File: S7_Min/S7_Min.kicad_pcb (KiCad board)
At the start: 4 copper layers, 124 parts, among them J1 Barrel_Jack_Switch, J2 XILINX_JTAG, Q1 DMN2020L, Q2 DMN63D8LDW, Q3 DMN63D8LDW, Q4 DMN63D8LDW, U1 TPS65581, U2 XC7S50-FTGB196, U3 REF3012, U4 QSPI_Flash_SOIC8, U5 MT47H128M16XX, X1 DSC61XX

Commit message: WIP
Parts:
- C2, C33, C45, C46, C5, R36, R37: moved to B.Cu
- moved C5 110.6 mm to (138.0, 94.2)
- moved C33 100.0 mm to (140.5, 95.5), turned to 180 degrees
- moved C2 98.6 mm to (143.0, 94.8), turned to 180 degrees
- moved C45 66.1 mm to (109.9, 93.3), turned to 270 degrees
- moved R37 65.3 mm to (109.4, 94.8), turned to 180 degrees
- moved C46 61.8 mm to (110.9, 93.3), turned to 270 degrees
- moved R36 59.6 mm to (108.9, 96.8), turned to 270 degrees
- moved C11 5.14 mm to (138.0, 96.5)
- moved C6 2.55 mm to (143.0, 97.0)
- moved C10 1.49 mm to (143.0, 93.0), turned to 270 degrees
- moved C4 1.00 mm to (143.0, 98.0)
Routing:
- net Net-(C45-Pad1): track 0.00 -> 8.08 mm, vias 0 -> 1
- net GND: track 62.3 -> 60.3 mm, vias 70 -> 71
- net +1V8: track 27.6 -> 28.7 mm
- added copper zone on B.Cu, net GND

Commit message: WIP
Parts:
- added C62: 10 uF, Capacitor_SMD:C_0805_2012Metric, F.Cu at (156.5, 35.0)
- added C63: 22 uF, Capacitor_SMD:C_0805_2012Metric, F.Cu at (156.5, 32.0)
- added C64: 0.1uF, Capacitor_SMD:C_0402_1005Metric, F.Cu at (92.0, 42.1)
- added C65: 0.1uF, Capacitor_SMD:C_0402_1005Metric, F.Cu at (88.4, 44.5)
- added C66: 0.1uF, Capacitor_SMD:C_0402_1005Metric, F.Cu at (94.9, 42.9)
- added C67: 0.1uF, Capacitor_SMD:C_0402_1005Metric, F.Cu at (91.3, 44.5)
- added D4: BAS16XV2T1G, Diode_SMD:D_SOD-523, F.Cu at (88.7, 42.3)
- added J3: HDMI_A, my_parts:hdmi_type_a_10029449-111RLF, F.Cu at (97.5, 32.0)
- added J4: Conn_02x12_Odd_Even, Connector_PinHeader_2.54mm:PinHeader_2x12_P2.54mm_Vertical, F.Cu at (82.1, 32.9)
- added R41: 47K, Resistor_SMD:R_0402_1005Metric, F.Cu at (88.4, 46.5)
- added R42: 47K, Resistor_SMD:R_0402_1005Metric, F.Cu at (88.4, 48.5)
- added R43: 47K, Resistor_SMD:R_0402_1005Metric, F.Cu at (84.1, 64.2)
- added R44: 100K, Resistor_SMD:R_0402_1005Metric, F.Cu at (91.3, 46.5)
- added R45: 10K, Resistor_SMD:R_0402_1005Metric, F.Cu at (88.4, 50.5)
- added R46: 49.9, Resistor_SMD:R_0402_1005Metric, F.Cu at (81.2, 64.2)
- added R47: 49.9, Resistor_SMD:R_0402_1005Metric, F.Cu at (97.8, 42.1)
- added R48: 49.9, Resistor_SMD:R_0402_1005Metric, F.Cu at (91.3, 48.5)
- added R49: 49.9, Resistor_SMD:R_0402_1005Metric, F.Cu at (94.2, 44.9)
- added R50: 49.9, Resistor_SMD:R_0402_1005Metric, F.Cu at (97.1, 44.9)
- added R51: 49.9, Resistor_SMD:R_0402_1005Metric, F.Cu at (100.0, 44.1)
- added R52: 49.9, Resistor_SMD:R_0402_1005Metric, F.Cu at (103.0, 42.1)
- added R53: 49.9, Resistor_SMD:R_0402_1005Metric, F.Cu at (103.0, 44.1)
- added R54: 27K, Resistor_SMD:R_0402_1005Metric, F.Cu at (100.0, 46.1)
- added R55: 2.2K, Resistor_SMD:R_0402_1005Metric, F.Cu at (94.2, 46.9)
- added R56: 2.2K, Resistor_SMD:R_0402_1005Metric, F.Cu at (97.1, 46.9)
- added R57: 10K, Resistor_SMD:R_0402_1005Metric, F.Cu at (94.2, 48.9)
- added U6: AZ1117-5.0, Package_TO_SOT_SMD:SOT-223-3_TabPin2, F.Cu at (149.4, 34.7)
- added U7: TPD12S521, Package_SO:TSSOP-38_4.4x9.7mm_P0.5mm, F.Cu at (117.0, 113.0)
- C16, C17, C18, C22, C26, C28, C29, C30, C32, RN1: moved to B.Cu
- moved J2 119.2 mm to (140.9, 115.1), turned to 90 degrees
- moved C28 103.3 mm to (140.8, 98.0), turned to 270 degrees
- moved C32 98.7 mm to (142.0, 93.0), turned to 270 degrees
- moved C29 96.2 mm to (140.0, 92.3)
- moved C30 94.5 mm to (140.8, 90.0), turned to 90 degrees
- moved RN1 93.1 mm to (139.9, 110.4), turned to 270 degrees
- moved C26 19.6 mm to (142.0, 97.0), turned to 90 degrees
- moved C16 18.8 mm to (142.0, 91.0)
- moved C22 17.2 mm to (143.0, 92.0)
- moved C18 14.9 mm to (138.0, 91.0), turned to 90 degrees
- moved C17 14.7 mm to (139.0, 91.0)
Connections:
- net Net-(U2-PadP9) renamed /Bank0_14/FPGA_DONE
- U2 pad H13: Net-(U2-PadH13) -> /Bank0_14/SYSRESET
- U2 pad H14: Net-(U2-PadH14) -> HDMI_SDA
- U2 pad K12: Net-(U2-PadK12) -> HDMI_CEC
- U2 pad M10: Net-(U2-PadM10) -> HDMI_HPD
- U2 pad M11: Net-(U2-PadM11) -> HDMI_D1+
- U2 pad M12: Net-(U2-PadM12) -> HDMI_D1-
- U2 pad M14: Net-(U2-PadM14) -> HDMI_CLK-
- U2 pad N11: Net-(U2-PadN11) -> HDMI_SCL
- U2 pad N14: Net-(U2-PadN14) -> HDMI_CLK+
- U2 pad P10: /Bank0_14/SYSRESET -> HDMI_D2+
- U2 pad P11: Net-(U2-PadP11) -> HDMI_D2-
- U2 pad P12: Net-(U2-PadP12) -> HDMI_D0+
- U2 pad P13: Net-(U2-PadP13) -> HDMI_D0-
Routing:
- net /Bank0_14/JTAG_TCK: track 0.00 -> 28.2 mm, vias 0 -> 1
- net /Bank0_14/JTAG_TMS: track 0.00 -> 16.6 mm, vias 0 -> 1
- net /Bank0_14/JTAG_TDI: track 0.00 -> 15.1 mm, vias 0 -> 1
- net GND: track 60.3 -> 74.4 mm, vias 71 -> 75
- net /Bank0_14/JTAG_TDO: track 0.00 -> 14.1 mm, vias 0 -> 1
- net +3V3: track 3.54 -> 10.8 mm, vias 5 -> 8
- net /Bank0_14/SPI_F_DQ3: track 0.00 -> 0.71 mm, vias 0 -> 1
- net /Bank0_14/SPI_F_DQ2: track 0.00 -> 0.71 mm, vias 0 -> 1
- net /Bank0_14/SPI_CS: track 0.00 -> 0.71 mm, vias 0 -> 1
- net GNDA: vias 4 -> 3
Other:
- net class Default: trace_width 0.25 -> 0.15

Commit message: WIP
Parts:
- added D5: FPGA_DONE, LED_SMD:LED_0805_2012Metric, F.Cu at (163.1, 108.5)
- added Q5: DMN2020L, Package_TO_SOT_SMD:SOT-23, F.Cu at (157.8, 105.7)
- added R58: 330, Resistor_SMD:R_0805_2012Metric_Pad1.15x1.40mm_HandSolder, F.Cu at (157.9, 108.5)
- added R59: 680, Resistor_SMD:R_0805_2012Metric_Pad1.15x1.40mm_HandSolder, F.Cu at (163.0, 104.7)
- R46, R47, R50, R51: moved to B.Cu
- moved S2 129.1 mm to (156.0, 115.2), turned to 180 degrees
- moved R16 94.5 mm to (143.5, 108.2)
- moved R17 93.0 mm to (146.0, 108.2), turned to 180 degrees
- moved J3 80.8 mm to (100.1, 112.8), turned to 270 degrees
- moved R47 77.0 mm to (118.4, 116.3)
- moved R49 75.0 mm to (120.9, 115.0), turned to 180 degrees
- moved R48 73.8 mm to (120.9, 116.1), turned to 180 degrees
- moved R52 73.3 mm to (120.9, 113.1), turned to 180 degrees
- moved R51 73.0 mm to (118.4, 114.7)
- moved R50 71.6 mm to (118.4, 113.3)
- moved R53 70.3 mm to (120.9, 112.0), turned to 180 degrees
- moved R46 65.2 mm to (118.4, 117.7)
- moved U7 2.96 mm to (114.5, 114.5), turned to 180 degrees
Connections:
- U2 pad H14: HDMI_SDA -> Net-(U2-PadH14)
- U2 pad M11: HDMI_D1+ -> HDMI_CLK+
- U2 pad M12: HDMI_D1- -> HDMI_CLK-
- U2 pad M14: HDMI_CLK- -> HDMI_SCL
- U2 pad N10: Net-(U2-PadN10) -> HDMI_D0+
- U2 pad N11: HDMI_SCL -> HDMI_D0-
- U2 pad N14: HDMI_CLK+ -> HDMI_SDA
- U2 pad P10: HDMI_D2+ -> HDMI_D1+
- U2 pad P11: HDMI_D2- -> HDMI_D1-
- U2 pad P12: HDMI_D0+ -> HDMI_D2+
- U2 pad P13: HDMI_D0- -> HDMI_D2-
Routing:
- net HDMI_D2-: track 0.00 -> 55.5 mm, vias 0 -> 2
- net HDMI_D2+: track 0.00 -> 55.4 mm, vias 0 -> 2
- net HDMI_CLK+: track 0.00 -> 54.3 mm, vias 0 -> 2
- net HDMI_CLK-: track 0.00 -> 54.3 mm, vias 0 -> 2
- net HDMI_D0-: track 0.00 -> 53.0 mm, vias 0 -> 2
- net HDMI_D0+: track 0.00 -> 53.0 mm, vias 0 -> 2
- net HDMI_D1+: track 0.00 -> 52.7 mm, vias 0 -> 2
- net HDMI_D1-: track 0.00 -> 52.5 mm, vias 0 -> 2
- net /Bank0_14/PROGRAM_B: track 0.00 -> 33.2 mm
- net /Bank0_14/FPGA_DONE: track 0.00 -> 20.7 mm
- net GND: track 74.4 -> 89.6 mm, vias 75 -> 87
- net /Bank0_14/INIT_B: track 0.00 -> 8.08 mm
- net +3V3: track 10.8 -> 15.5 mm, vias 8 -> 10
- net Net-(Q5-Pad3): track 0.00 -> 4.10 mm
- net Net-(D5-Pad2): track 0.00 -> 3.80 mm

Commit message: wip
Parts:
- added H1: MountingHole_Pad, MountingHole:MountingHole_3.2mm_M3_Pad_Via, F.Cu at (96.1, 59.8)
- added H2: MountingHole_Pad, MountingHole:MountingHole_3.2mm_M3_Pad_Via, F.Cu at (165.1, 59.8)
- added H3: MountingHole_Pad, MountingHole:MountingHole_3.2mm_M3_Pad_Via, F.Cu at (165.1, 126.8)
- added H4: MountingHole_Pad, MountingHole:MountingHole_3.2mm_M3_Pad_Via, F.Cu at (96.1, 126.8)
- C64, D4, R41, R42, R43, R44, R54, R55, R56, R57: moved to B.Cu
- moved C65 81.8 mm to (123.4, 118.5)
- moved C64 79.9 mm to (115.2, 118.5), turned to 90 degrees
- moved C67 76.9 mm to (108.4, 119.5)
- moved C66 76.8 mm to (108.4, 118.5)
- moved R45 75.3 mm to (120.8, 118.5)
- moved R41 72.7 mm to (120.9, 111.5), turned to 180 degrees
- moved C14 72.6 mm to (112.8, 61.7), turned to 180 degrees
- moved L1 70.7 mm to (112.1, 77.2), turned to 180 degrees
- moved U1 70.6 mm to (115.4, 67.5), turned to 90 degrees
- moved R42 68.8 mm to (117.1, 111.0)
- moved L2 68.6 mm to (110.2, 58.2), turned to 180 degrees
- moved R44 68.5 mm to (117.1, 110.0)
- moved D4 65.9 mm to (106.3, 105.8), turned to 90 degrees
- moved R54 62.9 mm to (106.3, 108.6), turned to 90 degrees
- moved R55 62.5 mm to (104.3, 108.6), turned to 90 degrees
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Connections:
- net Net-(C13-Pad1) renamed /Power/SW1
- net Net-(C14-Pad1) renamed /Power/SW2
- net Net-(C15-Pad1) renamed /Power/SW3
- C7 pad 1: Net-(C7-Pad1) -> +12V
- C8 pad 1: Net-(C7-Pad1) -> +12V
- C9 pad 1: Net-(C7-Pad1) -> +12V
- U1 pad 1: Net-(C7-Pad1) -> +12V
- U1 pad 2: Net-(C7-Pad1) -> +12V
- U2 pad K12: HDMI_CEC -> Net-(U2-PadK12)
- U2 pad L12: Net-(U2-PadL12) -> HDMI_CEC
- U2 pad M13: Net-(U2-PadM13) -> HDMI_SCL
- U2 pad M14: HDMI_SCL -> Net-(U2-PadM14)
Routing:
- net HDMI_CEC: track 0.00 -> 43.7 mm, vias 0 -> 3
- net HDMI_SCL: track 0.00 -> 40.9 mm, vias 0 -> 3
- net HDMI_SDA: track 0.00 -> 38.5 mm, vias 0 -> 3
- net HDMI_HPD: track 0.00 -> 33.7 mm, vias 0 -> 3
- net +3V3: track 15.5 -> 41.9 mm, vias 10 -> 15
- net GND: track 89.6 -> 108.2 mm, vias 87 -> 94
- net /Externals/HDMI_C_CEC: track 0.00 -> 13.9 mm, vias 0 -> 1
- net /Externals/HDMI_C_SCL: track 0.00 -> 13.1 mm, vias 0 -> 1
- net /Externals/HDMI_C_HPD: track 0.00 -> 12.9 mm, vias 0 -> 1
- net /Externals/HDMI_C_SDA: track 0.00 -> 12.6 mm, vias 0 -> 1
- net +1V0: track 9.19 -> 15.6 mm
- net /Externals/HDMI_C_5V: track 0.00 -> 4.62 mm, vias 0 -> 2
- net +5V: track 0.00 -> 4.02 mm, vias 0 -> 2
- net Net-(R45-Pad1): track 0.00 -> 3.02 mm
- net Net-(C66-Pad2): track 0.00 -> 2.71 mm
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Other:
- board outline added: 78 x 76 mm

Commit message: WIP
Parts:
- C37, C39, C40, C41, C42, C43, C44: moved to B.Cu
- S3: value CFG_RESET -> SYS_RESET
- moved C37 116.1 mm to (154.6, 97.6)
- moved C41 107.7 mm to (146.0, 94.0), turned to 180 degrees
- moved C42 102.0 mm to (147.0, 98.0)
- moved C39 94.8 mm to (155.7, 95.3)
- moved C40 94.3 mm to (153.1, 95.2)
- moved C44 93.4 mm to (146.0, 100.0), turned to 180 degrees
- moved R7 87.4 mm to (121.9, 56.5), turned to 270 degrees
- moved C43 85.1 mm to (147.0, 97.0)
- moved R4 74.6 mm to (122.9, 59.9)
- moved R5 69.8 mm to (117.9, 78.7), turned to 90 degrees
- moved C25 69.3 mm to (127.1, 56.3), turned to 270 degrees
- moved R2 64.9 mm to (119.0, 75.3)
- moved C19 60.2 mm to (108.7, 82.0), turned to 180 degrees
- moved C21 58.4 mm to (124.8, 56.3), turned to 270 degrees
- moved C23 56.5 mm to (108.7, 80.0), turned to 180 degrees
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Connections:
- U2 pad J12: /Bank0_14/RGB2_G -> /Bank0_14/RGB2_B
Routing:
- net Net-(R4-Pad1): track 0.00 -> 10.4 mm
- net Net-(C13-Pad2): track 0.00 -> 3.41 mm
- net /Externals/HDMI_C_CEC: track 13.9 -> 17.1 mm
- net /Externals/HDMI_C_HPD: track 12.9 -> 16.1 mm
- net /Externals/HDMI_C_SCL: track 13.1 -> 16.3 mm
- net /Externals/HDMI_C_SDA: track 12.6 -> 15.7 mm
- net Net-(C15-Pad2): track 0.00 -> 3.03 mm
- net Net-(C14-Pad2): track 0.00 -> 3.03 mm
- net Net-(R1-Pad1): track 0.00 -> 3.00 mm, vias 0 -> 2
- net GND: track 108.2 -> 105.8 mm, vias 94 -> 89
- net /Externals/HDMI_C_5V: track 4.62 -> 2.92 mm, vias 2 -> 1
- net Net-(R3-Pad1): track 0.00 -> 1.50 mm, vias 0 -> 1
- net HDMI_CEC: track 43.7 -> 44.9 mm
- net HDMI_D0-: track 53.0 -> 54.1 mm
- net HDMI_D2-: track 55.5 -> 56.6 mm
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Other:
- board size 78 x 76 mm -> 78 x 72 mm
- net class Default: via_drill 0.3 -> 0.25
- net class HDMI_DIFF added: clearance 0.1, trace_width 0.15, via_dia 0.45, via_drill 0.2
- net class Power: via_drill 0.3 -> 0.25

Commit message: WIP
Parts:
- C35, C36, RN2: moved to B.Cu
- moved U4 91.5 mm to (143.8, 78.2)
- moved C36 88.9 mm to (144.1, 77.5), turned to 180 degrees
- moved R27 88.1 mm to (150.1, 77.6)
- moved R33 86.7 mm to (141.5, 84.0)
- moved R29 85.3 mm to (137.5, 77.6), turned to 180 degrees
- moved R28 85.2 mm to (137.5, 78.9), turned to 180 degrees
- moved C35 76.8 mm to (144.1, 76.3), turned to 180 degrees
- moved C20 42.5 mm to (142.6, 62.0), turned to 0 degrees
- moved C24 40.8 mm to (142.6, 64.3), turned to 0 degrees
- moved C27 39.3 mm to (142.6, 66.7), turned to 0 degrees
- moved R6 29.3 mm to (136.1, 60.9), turned to 180 degrees
- moved R3 26.7 mm to (132.7, 59.8), turned to 90 degrees
- moved L2 25.4 mm to (135.5, 65.3), turned to 0 degrees
- moved R7 23.9 mm to (136.1, 75.7), turned to 180 degrees
- moved L3 22.9 mm to (135.5, 71.3), turned to 0 degrees
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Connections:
- RN2 pad 1: /Bank0_14/SPI_DQ0 -> /Bank0_14/SPI_DQ2
- RN2 pad 2: /Bank0_14/SPI_DQ1 -> /Bank0_14/SPI_DQ3
- RN2 pad 3: /Bank0_14/SPI_DQ2 -> /Bank0_14/SPI_DQ0
- RN2 pad 4: /Bank0_14/SPI_DQ3 -> /Bank0_14/SPI_DQ1
- RN2 pad 5: /Bank0_14/SPI_F_DQ3 -> /Bank0_14/SPI_F_DQ1
- RN2 pad 6: /Bank0_14/SPI_F_DQ2 -> /Bank0_14/SPI_F_DQ0
- RN2 pad 7: /Bank0_14/SPI_F_DQ1 -> /Bank0_14/SPI_F_DQ3
- RN2 pad 8: /Bank0_14/SPI_F_DQ0 -> /Bank0_14/SPI_F_DQ2
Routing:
- net /Bank0_14/SPI_CS: track 0.71 -> 21.5 mm, vias 1 -> 2
- net /Bank0_14/SPI_SCLK: track 0.00 -> 12.7 mm
- net /Bank0_14/SPI_DQ3: track 0.00 -> 12.4 mm, vias 0 -> 1
- net /Bank0_14/SPI_DQ1: track 0.00 -> 9.96 mm, vias 0 -> 1
- net /Bank0_14/SPI_DQ2: track 0.00 -> 9.87 mm, vias 0 -> 1
- net +3V3: track 41.9 -> 48.5 mm, vias 14 -> 16
- net /Bank0_14/SPI_DQ0: track 0.00 -> 6.50 mm, vias 0 -> 1
- net GND: track 105.8 -> 111.3 mm, vias 89 -> 91
- net /Bank0_14/SPI_F_DQ2: track 0.71 -> 5.91 mm
- net /Bank0_14/SPI_F_DQ1: track 0.00 -> 4.12 mm, vias 0 -> 1
- net /Bank0_14/SPI_F_SCLK: track 0.00 -> 4.01 mm
- net /Bank0_14/SPI_F_DQ3: track 0.71 -> 4.71 mm
- net /Bank0_14/SPI_F_DQ0: track 0.00 -> 3.91 mm, vias 0 -> 1

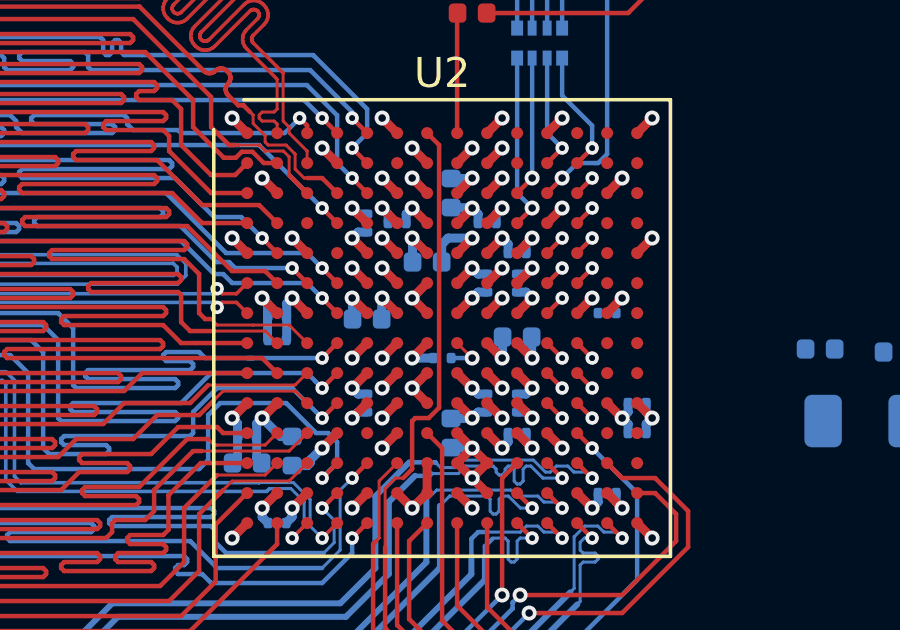
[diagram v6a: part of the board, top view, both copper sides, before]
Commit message: changed package of 2 ADC capacitors to 0402 from 0201 to eliminate a BOM line
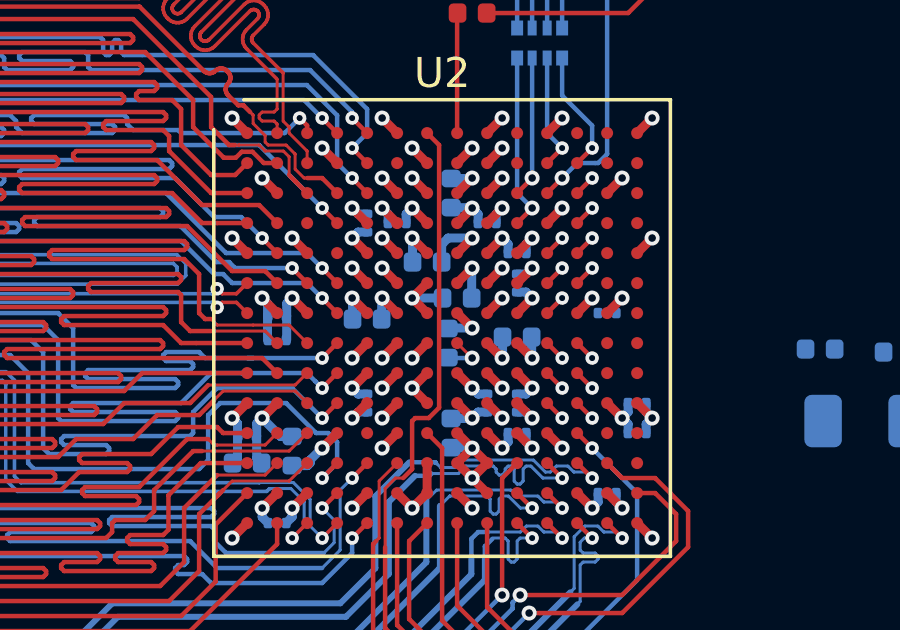
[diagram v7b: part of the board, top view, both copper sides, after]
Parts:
- C32, C33: footprint my_parts:C_0201_0603Metric -> Capacitor_SMD:C_0402_1005Metric
- moved C32 1.12 mm to (141.0, 93.5), turned to 180 degrees
- moved C33 0.54 mm to (140.7, 95.0), turned to 90 degrees
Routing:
- net GNDA: track 4.11 -> 4.65 mm
